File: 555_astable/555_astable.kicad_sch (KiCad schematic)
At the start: 9 parts, among them J1 Conn_01x02, J2 Conn_01x03, SW1 SW_SPST, U1 NE555P

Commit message: actualizar 555 oficial
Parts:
- added J3: Conn_01x02, TerminalBlock:TerminalBlock_MaiXu_MX126-5.0-02P_1x02_P5.00mm, symbol Connector_Generic:Conn_01x02
- SW1: footprint Button_Switch_THT:SW_CK_JS202011CQN_DPDT_Straight -> Button_Switch_THT:SW_E-Switch_EG1271_SPDT
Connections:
- net GND: now also J3.2 (Pin_2)
- net VCC: now also J3.1 (Pin_1)
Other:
- note added: "patitas de 555: 1: a GND (+) 2: a GND (+) por C de 10n, a patita 3 de pote-1 3: a R 10k hacia (+) LED y LED a VCC (-). 3: a pin 14 de 4017 4: a VCC (-) 5: a GND (+) por C de 100n 6: a patita 2 7: a VCC (-) por R 10k, a patita 2 de pote-1 8: a VCC (-) J1: alimentación + switch J2: salida potenciómetro + salida output pin 3 J3: salida alimentación a 4017"
- note removed: "patitas de 555: 1: a GND (+) 2: a GND (+) por C de 10n, a patita 3 de pote-1 3: a R 10k hacia (+) LED y LED a VCC (-). 3: a pin 14 de 4017 4: a VCC (-) 5: a GND (+) por C de 100n 6: a patita 2 7: a VCC (-) por R 10k, a patita 2 de pote-1 8: a VCC (-)"
- moved on the sheet: J1, SW1
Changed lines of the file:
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@@
 		(rev "v1")
 	)
-	(text "patitas de 555:\n1: a GND (+)\n2: a GND (+) por C de 10n, a patita 3 de pote-1\n3: a R 10k hacia (+) LED y LED a VCC (-). \n3: a pin 14 de 4017\n4: a VCC (-)\n5: a GND (+) por C de 100n\n6: a patita 2\n7: a VCC (-) por R 10k, a patita 2 de pote-1\n8: a VCC (-)"
-		(exclude_from_sim no)
-		(at 14.478 121.412 0)
+	(text "patitas de 555:\n\n1: a GND (+)\n2: a GND (+) por C de 10n, a patita 3 de pote-1\n3: a R 10k hacia (+) LED y LED a VCC (-). \n3: a pin 14 de 4017\n4: a VCC (-)\n5: a GND (+) por C de 100n\n6: a patita 2\n7: a VCC (-) por R 10k, a patita 2 de pote-1\n8: a VCC (-)\n\nJ1: alimentación + switch\nJ2: salida potenciómetro + salida output pin 3\nJ3: salida alimentación a 4017"
+		(exclude_from_sim no)
+		(at 14.224 115.57 0)
 		(effects
 			(font
@@
 	(wire
 		(pts
-			(xy 134.62 66.04) (xy 137.16 66.04)
+			(xy 134.62 66.04) (xy 135.89 66.04)
 		)
 		(stroke
@@
 	(wire
 		(pts
-			(xy 125.73 76.2) (xy 125.73 78.74)
+			(xy 135.89 82.55) (xy 135.89 85.09)
 		)
 		(stroke
@@
 	(wire
 		(pts
-			(xy 143.51 76.2) (xy 143.51 78.74)
+			(xy 153.67 82.55) (xy 153.67 85.09)
 		)
 		(stroke
@@
 	(wire
 		(pts
-			(xy 139.7 76.2) (xy 143.51 76.2)
-		)
-		(stroke
-			(width 0)
-			(type default)
-		)
-	)
-	(wire
-		(pts
-			(xy 125.73 76.2) (xy 129.54 76.2)
+			(xy 149.86 82.55) (xy 153.67 82.55)
+		)
+		(stroke
+			(width 0)
+			(type default)
+		)
+	)
+	(wire
+		(pts
+			(xy 135.89 82.55) (xy 139.7 82.55)
 		)
 		(stroke
@@
 	(wire
 		(pts
-			(xy 143.51 81.28) (xy 125.73 81.28)
+			(xy 153.67 87.63) (xy 135.89 87.63)
 		)
 		(stroke
@@
 			(width 0)
 			(type default)
+		)
+	)
+	(label "GND"
+		(at 153.67 74.93 180)
+		(effects
+			(font
+				(size 1.27 1.27)
+			)
+			(justify right bottom)
+		)
+	)
+	(label "VCC"
+		(at 153.67 72.39 180)
+		(effects
+			(font
+				(size 1.27 1.27)
+			)
+			(justify right bottom)
 		)
 	)
@@
 	(symbol
 		(lib_id "Switch:SW_SPST")
-		(at 134.62 76.2 0)
+		(at 144.78 82.55 0)
 		(unit 1)
 		(body_style 1)
@@
 		(dnp no)
 		(property "Reference" "SW1"
-			(at 134.62 78.232 0)
+			(at 144.78 84.582 0)
 			(show_name no)
 			(do_not_autoplace no)
@@
 		)
 		(property "Value" "SW_SPST"
-			(at 134.62 72.898 0)
-			(show_name no)
-			(do_not_autoplace no)
-			(effects
-				(font
-					(size 1.27 1.27)
-				)
-			)
-		)
-		(property "Footprint" "Button_Switch_THT:SW_CK_JS202011CQN_DPDT_Straight"
-			(at 134.62 76.2 0)
+			(at 144.78 79.248 0)
+			(show_name no)
+			(do_not_autoplace no)
+			(effects
+				(font
+					(size 1.27 1.27)
+				)
+			)
+		)
+		(property "Footprint" "Button_Switch_THT:SW_E-Switch_EG1271_SPDT"
+			(at 144.78 82.55 0)
 			(hide yes)
 			(show_name no)
@@
 		)
 		(property "Datasheet" ""
-			(at 134.62 76.2 0)
+			(at 144.78 82.55 0)
 			(hide yes)
 			(show_name no)
@@
 		)
 		(property "Description" "Single Pole Single Throw (SPST) switch"
-			(at 134.62 76.2 0)
+			(at 144.78 82.55 0)
 			(hide yes)
 			(show_name no)
@@
 	(symbol
 		(lib_id "power:VCC")
-		(at 137.16 66.04 270)
+		(at 135.89 66.04 270)
 		(unit 1)
 		(body_style 1)
@@
 		(dnp no)
 		(property "Reference" "#PWR07"
-			(at 133.35 66.04 0)
+			(at 132.08 66.04 0)
 			(hide yes)
 			(show_name no)
@@
 		)
 		(property "Value" "VCC"
-			(at 140.208 66.04 90)
+			(at 138.938 66.04 90)
 			(show_name no)
 			(do_not_autoplace no)
@@
 		)
 		(property "Footprint" ""
-			(at 137.16 66.04 0)
+			(at 135.89 66.04 0)
 			(hide yes)
 			(show_name no)
@@
 		)
 		(property "Datasheet" ""
-			(at 137.16 66.04 0)
+			(at 135.89 66.04 0)
 			(hide yes)
 			(show_name no)
@@
 		)
 		(property "Description" "Power symbol creates a global label with name \"VCC\""
-			(at 137.16 66.04 0)
+			(at 135.89 66.04 0)
 			(hide yes)
 			(show_name no)
@@
 		(dnp no)
 		(property "Reference" "D1"
-			(at 130.302 60.706 0)
+			(at 130.81 62.992 0)
 			(show_name no)
 			(do_not_autoplace no)
@@
 		)
 		(property "Value" "LED"
-			(at 130.81 62.992 0)
+			(at 130.81 69.088 0)
 			(show_name no)
 			(do_not_autoplace no)
@@
 	(symbol
 		(lib_id "power:VCC")
-		(at 125.73 78.74 90)
+		(at 135.89 85.09 90)
 		(unit 1)
 		(body_style 1)
@@
 		(fields_autoplaced yes)
 		(property "Reference" "#PWR08"
-			(at 129.54 78.74 0)
+			(at 139.7 85.09 0)
 			(hide yes)
 			(show_name no)
@@
 		)
 		(property "Value" "VCC"
-			(at 121.92 78.7399 90)
+			(at 132.08 85.0899 90)
 			(show_name no)
 			(do_not_autoplace no)
@@
 		)
 		(property "Footprint" ""
-			(at 125.73 78.74 0)
+			(at 135.89 85.09 0)
 			(hide yes)
 			(show_name no)
@@
 		)
 		(property "Datasheet" ""
-			(at 125.73 78.74 0)
+			(at 135.89 85.09 0)
 			(hide yes)
 			(show_name no)
@@
 		)
 		(property "Description" "Power symbol creates a global label with name \"VCC\""
-			(at 125.73 78.74 0)
+			(at 135.89 85.09 0)
 			(hide yes)
 			(show_name no)
@@
 	(symbol
 		(lib_id "Connector_Generic:Conn_01x02")
-		(at 148.59 78.74 0)
+		(at 158.75 85.09 0)
 		(unit 1)
 		(body_style 1)
@@
 		(fields_autoplaced yes)
 		(property "Reference" "J1"
-			(at 151.13 78.7399 0)
+			(at 161.29 85.0899 0)
 			(show_name no)
 			(do_not_autoplace no)
@@
 		)
 		(property "Value" "Conn_01x02"
-			(at 151.13 81.2799 0)
+			(at 161.29 87.6299 0)
 			(show_name no)
 			(do_not_autoplace no)
@@
 		)
 		(property "Footprint" "TerminalBlock:TerminalBlock_MaiXu_MX126-5.0-02P_1x02_P5.00mm"
-			(at 148.59 78.74 0)
+			(at 158.75 85.09 0)
 			(hide yes)
 			(show_name no)
@@
 		)
 		(property "Datasheet" ""
-			(at 148.59 78.74 0)
+			(at 158.75 85.09 0)
 			(hide yes)
 			(show_name no)
@@
 		)
 		(property "Description" "Generic connector, single row, 01x02, script generated (kicad-library-utils/schlib/autogen/connector/)"
-			(at 148.59 78.74 0)
+			(at 158.75 85.09 0)
 			(hide yes)
 			(show_name no)
@@
 	(symbol
 		(lib_id "power:GND")
-		(at 125.73 81.28 270)
+		(at 135.89 87.63 270)
 		(unit 1)
 		(body_style 1)
@@
 		(fields_autoplaced yes)
 		(property "Reference" "#PWR09"
-			(at 119.38 81.28 0)
+			(at 129.54 87.63 0)
 			(hide yes)
 			(show_name no)
@@
 		)
 		(property "Value" "GND"
-			(at 121.92 81.2799 90)
+			(at 132.08 87.6299 90)
 			(show_name no)
 			(do_not_autoplace no)
@@
 		)
 		(property "Footprint" ""
-			(at 125.73 81.28 0)
+			(at 135.89 87.63 0)
 			(hide yes)
 			(show_name no)
@@
 		)
 		(property "Datasheet" ""
-			(at 125.73 81.28 0)
+			(at 135.89 87.63 0)
 			(hide yes)
 			(show_name no)
@@
 		)
 		(property "Description" "Power symbol creates a global label with name \"GND\" , ground"
-			(at 125.73 81.28 0)
+			(at 135.89 87.63 0)
 			(hide yes)
 			(show_name no)
@@
 		(dnp no)
 		(property "Reference" "C2"
-			(at 100.076 46.99 0)
+			(at 92.202 48.514 0)
 			(show_name no)
 			(do_not_autoplace no)
@@
 		)
 		(property "Value" "100n"
-			(at 93.472 46.99 0)
+			(at 91.44 50.546 0)
 			(show_name no)
 			(do_not_autoplace no)
@@
 					(unit 1)
 				)
+			)
+		)
+	)
+	(symbol
+		(lib_id "Connector_Generic:Conn_01x02")
+		(at 158.75 72.39 0)
+		(unit 1)
+		(body_style 1)
+		(exclude_from_sim no)
+		(in_bom yes)
+		(on_board yes)
+		(in_pos_files yes)
+		(dnp no)
+		(fields_autoplaced yes)
+		(property "Reference" "J3"
+			(at 161.29 72.3899 0)
+			(show_name no)
+			(do_not_autoplace no)
+			(effects
+				(font
+					(size 1.27 1.27)
+				)
+				(justify left)
+			)
+		)
+		(property "Value" "Conn_01x02"
+			(at 161.29 74.9299 0)
+			(show_name no)
+			(do_not_autoplace no)
+			(effects
+				(font
+					(size 1.27 1.27)
+				)
+				(justify left)
+			)
+		)
+		(property "Footprint" "TerminalBlock:TerminalBlock_MaiXu_MX126-5.0-02P_1x02_P5.00mm"
+			(at 158.75 72.39 0)
+			(hide yes)
+			(show_name no)
+			(do_not_autoplace no)
+			(effects
+				(font
+					(size 1.27 1.27)
+				)
+			)
+		)
+		(property "Datasheet" ""
+			(at 158.75 72.39 0)
+			(hide yes)
+			(show_name no)
+			(do_not_autoplace no)
+			(effects
+				(font
+					(size 1.27 1.27)
+				)
+			)
+		)
+		(property "Description" "Generic connector, single row, 01x02, script generated (kicad-library-utils/schlib/autogen/connector/)"
+			(at 158.75 72.39 0)
+			(hide yes)
+			(show_name no)
+			(do_not_autoplace no)
+			(effects
+				(font
+					(size 1.27 1.27)
+				)
+			)
+		)
+		(pin "1"
+		)
+		(pin "2"
+		)
+		(instances
+			(project "555_astable"
+				(path "/f0997c31-ec15-4e60-aae3-7d657b633fbd"
+					(reference "J3")
+					(unit 1)
+				)

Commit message: fix 555 + design 4017
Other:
- note added: "patitas de 555: 1: a GND (+) 2: a GND (+) por C de 10n, a patita 3 de pote (J2) 3: a R 10k hacia (+) LED y LED a VCC (-). 3: a pin 14 de 4017 4: a VCC (-) 5: a GND (+) por C de 100n 6: a patita 2 7: a VCC (-) por R 10k, a patita 2 de pote (J2) 8: a VCC (-) J1: alimentación + switch J2: salida potenciómetro + salida output pin 3 J3: salida alimentación a 4017"
- note removed: "patitas de 555: 1: a GND (+) 2: a GND (+) por C de 10n, a patita 3 de pote-1 3: a R 10k hacia (+) LED y LED a VCC (-). 3: a pin 14 de 4017 4: a VCC (-) 5: a GND (+) por C de 100n 6: a patita 2 7: a VCC (-) por R 10k, a patita 2 de pote-1 8: a VCC (-) J1: alimentación + switch J2: salida potenciómetro + salida output pin 3 J3: salida alimentación a 4017"
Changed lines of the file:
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@@
 		(rev "v1")
 	)
-	(text "patitas de 555:\n\n1: a GND (+)\n2: a GND (+) por C de 10n, a patita 3 de pote-1\n3: a R 10k hacia (+) LED y LED a VCC (-). \n3: a pin 14 de 4017\n4: a VCC (-)\n5: a GND (+) por C de 100n\n6: a patita 2\n7: a VCC (-) por R 10k, a patita 2 de pote-1\n8: a VCC (-)\n\nJ1: alimentación + switch\nJ2: salida potenciómetro + salida output pin 3\nJ3: salida alimentación a 4017"
+	(text "patitas de 555:\n\n1: a GND (+)\n2: a GND (+) por C de 10n, a patita 3 de pote (J2)\n3: a R 10k hacia (+) LED y LED a VCC (-). \n3: a pin 14 de 4017\n4: a VCC (-)\n5: a GND (+) por C de 100n\n6: a patita 2\n7: a VCC (-) por R 10k, a patita 2 de pote (J2)\n8: a VCC (-)\n\nJ1: alimentación + switch\nJ2: salida potenciómetro + salida output pin 3\nJ3: salida alimentación a 4017"
 		(exclude_from_sim no)
 		(at 14.224 115.57 0)

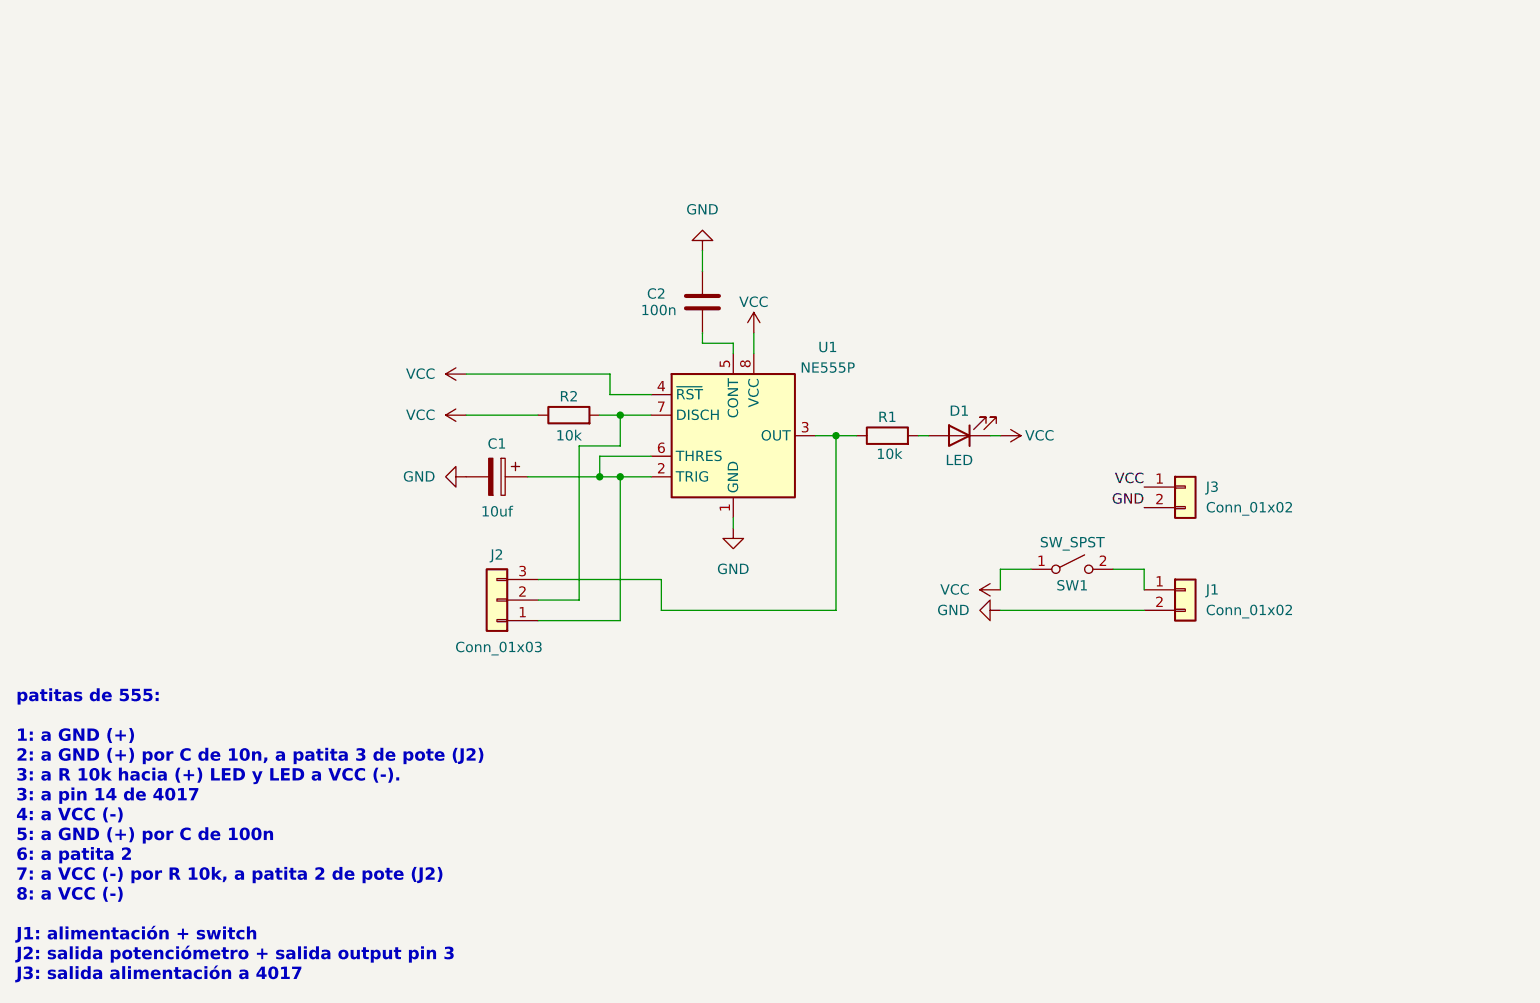
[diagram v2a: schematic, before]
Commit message: arreglar 4017 + iniciar 4093
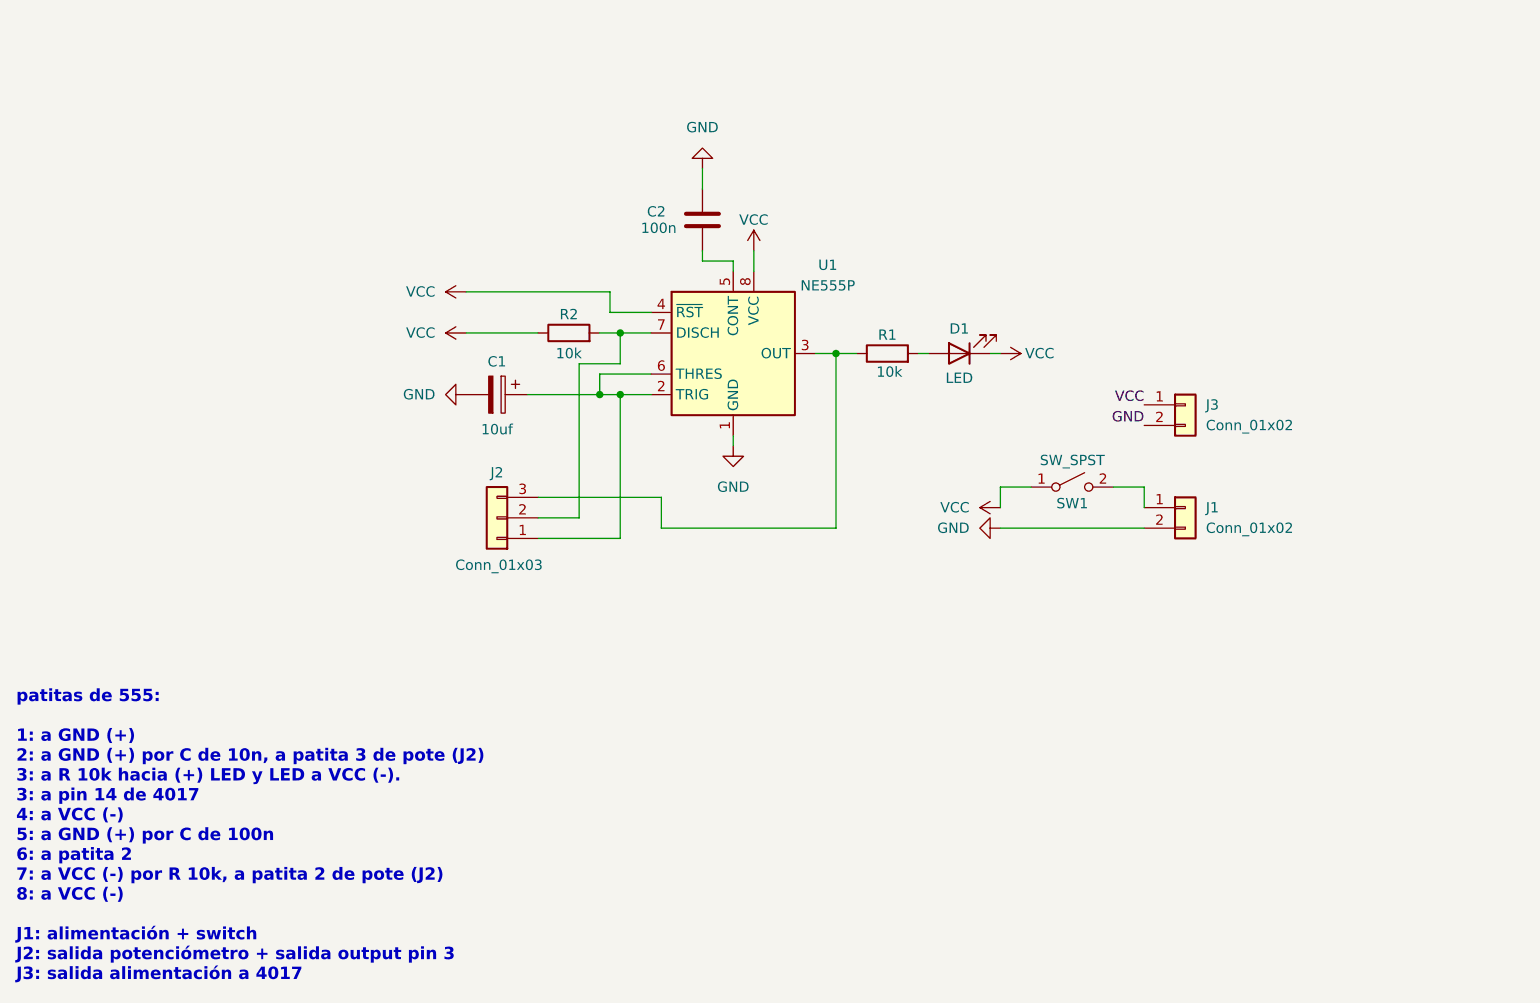
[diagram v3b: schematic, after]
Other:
- moved on the sheet: C1, C2, D1, J1, J2, J3, R1, R2, SW1, U1

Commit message: nueva version corregida de sch
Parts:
- removed C1: 10uf, Capacitor_THT:C_Radial_D5.0mm_H5.0mm_P2.00mm, symbol Device:C_Polarized
- removed C2: 100n, Capacitor_THT:C_Disc_D5.0mm_W2.5mm_P5.00mm, symbol Device:C
- removed J2: Conn_01x03, TerminalBlock:TerminalBlock_MaiXu_MX126-5.0-03P_1x03_P5.00mm, symbol Connector_Generic:Conn_01x03
- added C1: 100n, Capacitor_THT:C_Disc_D5.0mm_W2.5mm_P5.00mm, symbol Device:C
- added C2: 10uf, Capacitor_THT:C_Radial_D5.0mm_H5.0mm_P2.00mm, symbol Device:C_Polarized
- added J3: Conn_01x02, TerminalBlock:TerminalBlock_MaiXu_MX126-5.0-02P_1x02_P5.00mm, symbol Connector_Generic:Conn_01x02
- added RV1: 100k, TerminalBlock:TerminalBlock_MaiXu_MX126-5.0-02P_1x02_P5.00mm, symbol Device:R_Potentiometer
- renumbered J3 to J2
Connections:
- net GND: now also D1.1 (K), C1.1, C2.2, J3.2 (Pin_2)
- net VCC: now also R1.2; no longer D1.1 (K), R2.1
- net at U1.2 (TRIG), U1.6 (THRES): now also C2.1, RV1.3
- net at R1.1: now also U1.7 (DISCH), RV1.2; no longer U1.3 (OUT)
- net at U1.5 (CONT): now also C1.2
- net at R2.2: now also U1.3 (OUT), J3.1 (Pin_1); no longer U1.7 (DISCH)
- net at D1.2 (A): now also R2.1; no longer R1.2
- no-connect marks 0 -> 1
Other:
- note added: "entrada de fuente de poder con interruptor"
- note added: "patitas de 555: 1: a GND (+) 2: a GND (+) por C de 10n, a patita 3 de pote 3: a salida 3: a LED protegido por R de 10k 4: a VCC (-) 5: a GND (+) por C de 100n 6: a patita 2 7: a VCC (-) por R 10k, a patita 2 de pote 8: a VCC (-) J1: entrada de alimentación + switch J2: salida alimentación a 4017 J3: salida 555 astable"
- note added: "salida de chip 555 astable"
- note added: "salida de fuente de poder para alimentar otras placas"
- note removed: "patitas de 555: 1: a GND (+) 2: a GND (+) por C de 10n, a patita 3 de pote (J2) 3: a R 10k hacia (+) LED y LED a VCC (-). 3: a pin 14 de 4017 4: a VCC (-) 5: a GND (+) por C de 100n 6: a patita 2 7: a VCC (-) por R 10k, a patita 2 de pote (J2) 8: a VCC (-) J1: alimentación + switch J2: salida potenciómetro + salida output pin 3 J3: salida alimentación a 4017"
- moved on the sheet: J1, J2, SW1
